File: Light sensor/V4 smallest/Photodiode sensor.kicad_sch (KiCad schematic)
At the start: 11 parts, among them IC1 BH1730FVC-TR, J1 Conn_01x02, J2 Conn_01x04, J3 Conn_01x05

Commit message: Updated footprints
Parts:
- added C1: KAM21BR71H104JM, CAPC2012X94N, symbol CUSTOM_SYMBOL:KAM21BR71H104JM
- added C2: C1608X5R1E475K080AC, CAPC1608X80N, symbol CUSTOM_SYMBOL:C1608X5R1E475K080AC
- R1, R2, R3: value RC0402JR-073M3L -> RMCA1206FT4K70-HP; footprint CUSTOM_LIBRARY:RC0402JR-073M3L -> CUSTOM_LIBRARY:RMCA1206FT4K70-HP
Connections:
- net 3.3V: now also C1.1, C2.1
- net GND: now also C1.2, C2.2
- net INT 2: now also R1.1; no longer R3.1
- net SCL 2: now also R3.1; no longer R1.1

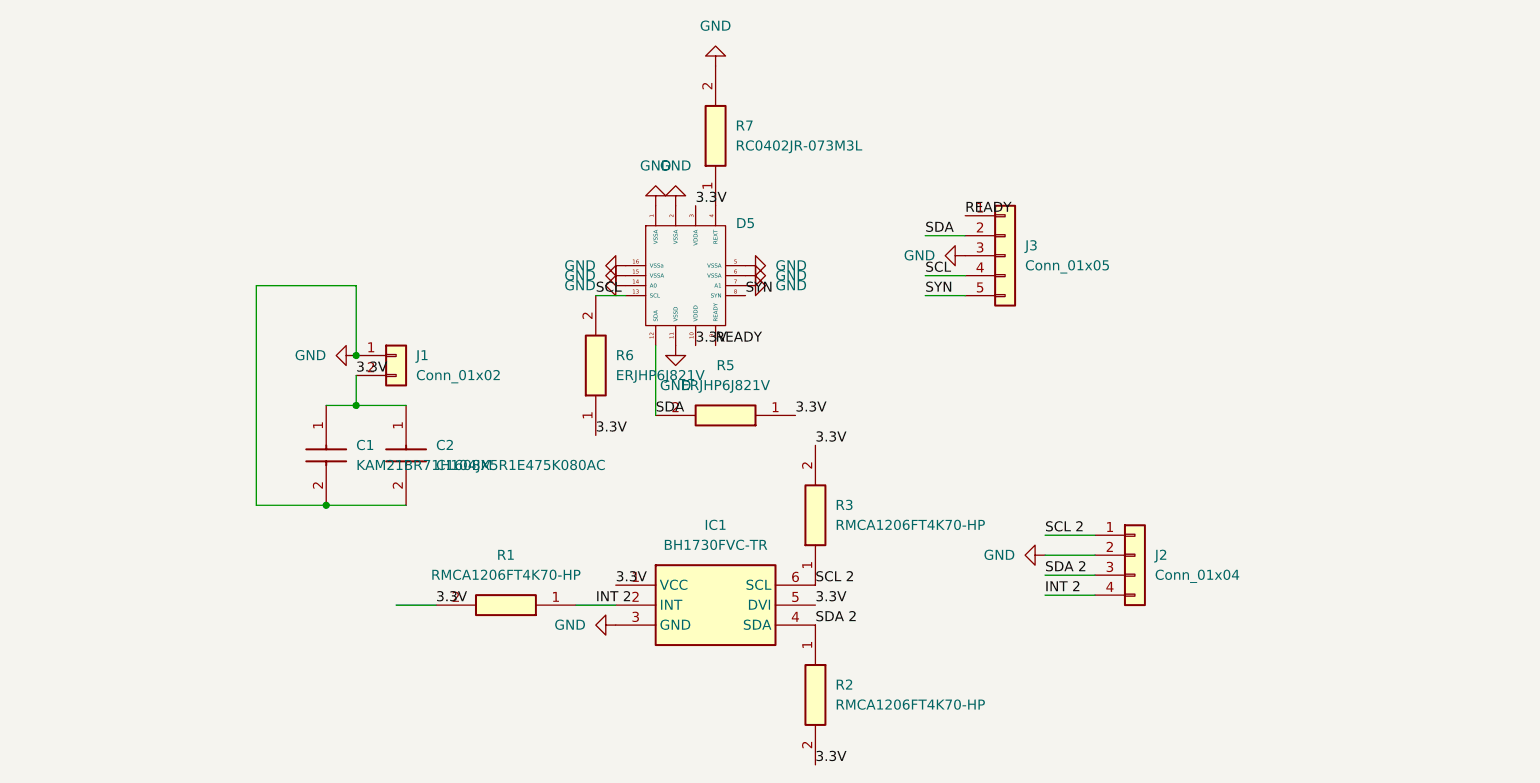
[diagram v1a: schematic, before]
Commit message: Changed V4 PCB
Connected both SCL and SDA pins together as they have different addresses. Made the PCB a lot smaller. Got a good connector placed on the bottom side of the PCB
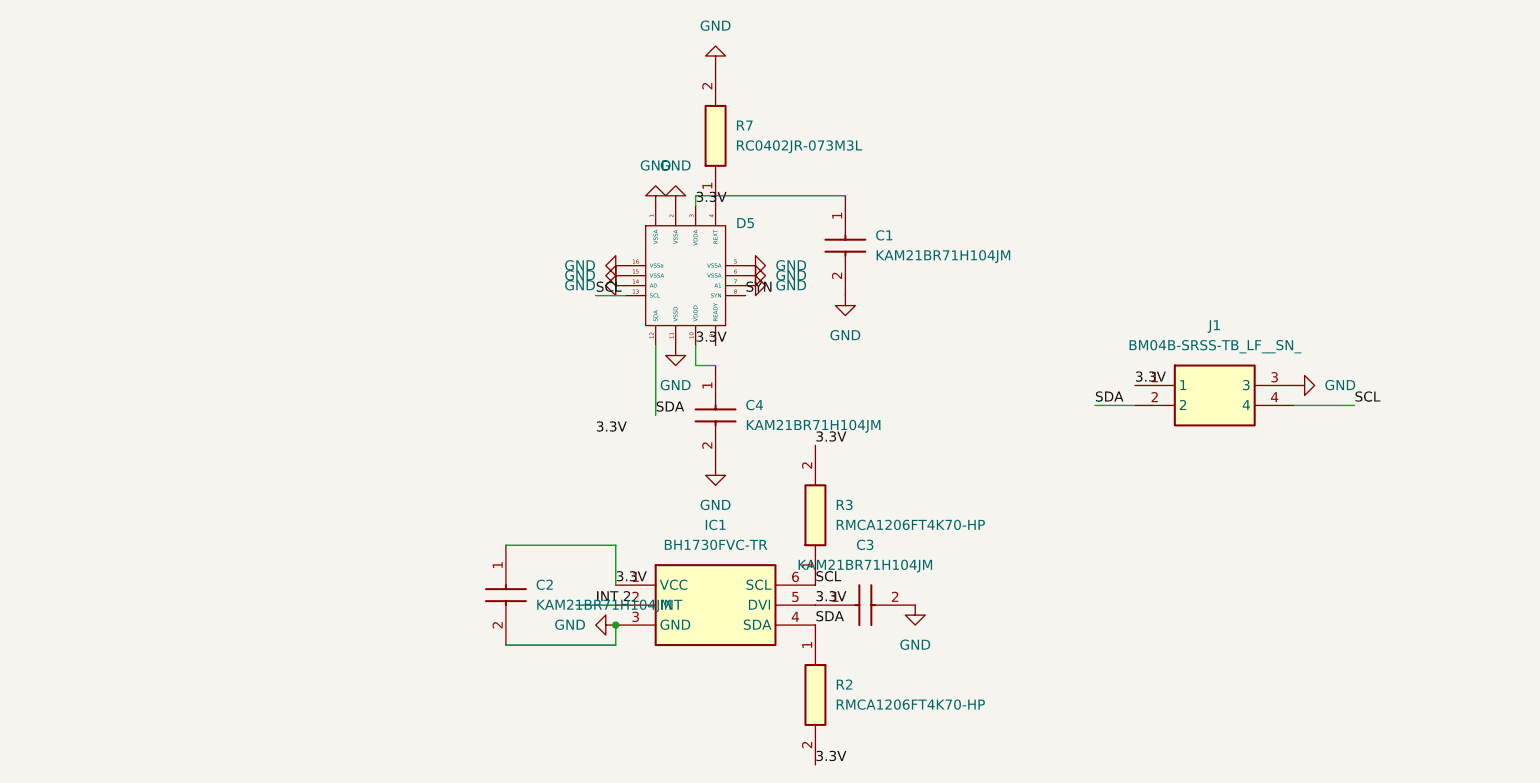
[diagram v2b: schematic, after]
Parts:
- removed C2: C1608X5R1E475K080AC, CAPC1608X80N, symbol CUSTOM_SYMBOL:C1608X5R1E475K080AC
- removed J1: Conn_01x02, Connector_PinHeader_1.00mm:PinHeader_1x02_P1.00mm_Vertical, symbol Connector_Generic:Conn_01x02
- removed J2: Conn_01x04, Connector_PinHeader_1.00mm:PinHeader_1x04_P1.00mm_Vertical, symbol Connector_Generic:Conn_01x04
- removed J3: Conn_01x05, Connector_PinHeader_1.00mm:PinHeader_1x05_P1.00mm_Vertical, symbol Connector_Generic:Conn_01x05
- removed R1: RMCA1206FT4K70-HP, CUSTOM_LIBRARY:RMCA1206FT4K70-HP, symbol CUSTOM_SYMBOL:RMCA1206FT4K70-HP
- removed R5, R6: ERJHP6J821V, ERJHP6D1000V, symbol CUSTOM_SYMBOL:ERJHP6J821V
- added C2, C3, C4: KAM21BR71H104JM, CAPC2012X94N, symbol CUSTOM_SYMBOL:KAM21BR71H104JM
- added J1: BM04B-SRSS-TB_LF__SN_, BM04B-SRSS-TB_LFSN_, symbol CUSTOM_SYMBOL:BM04B-SRSS-TB_LF__SN_
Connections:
- net SCL 2 is gone; now on net SCL: IC1.6 (SCL), R3.1
- net SDA 2 is gone; now on net SDA: IC1.4 (SDA), R2.1
- net 3.3V: now also C2.1, C3.1, C4.1, J1.1
- net GND: now also C2.2, C3.2, C4.2, J1.3
- net SCL: now also J1.4
- net SDA: now also J1.2
- net READY: no longer names the net of D5.9 (READY)
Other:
- moved on the sheet: C1

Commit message: Updated PCB components
Found in stock components and put onto the PCB. Need to double check against datasheet to ensure all connections are good
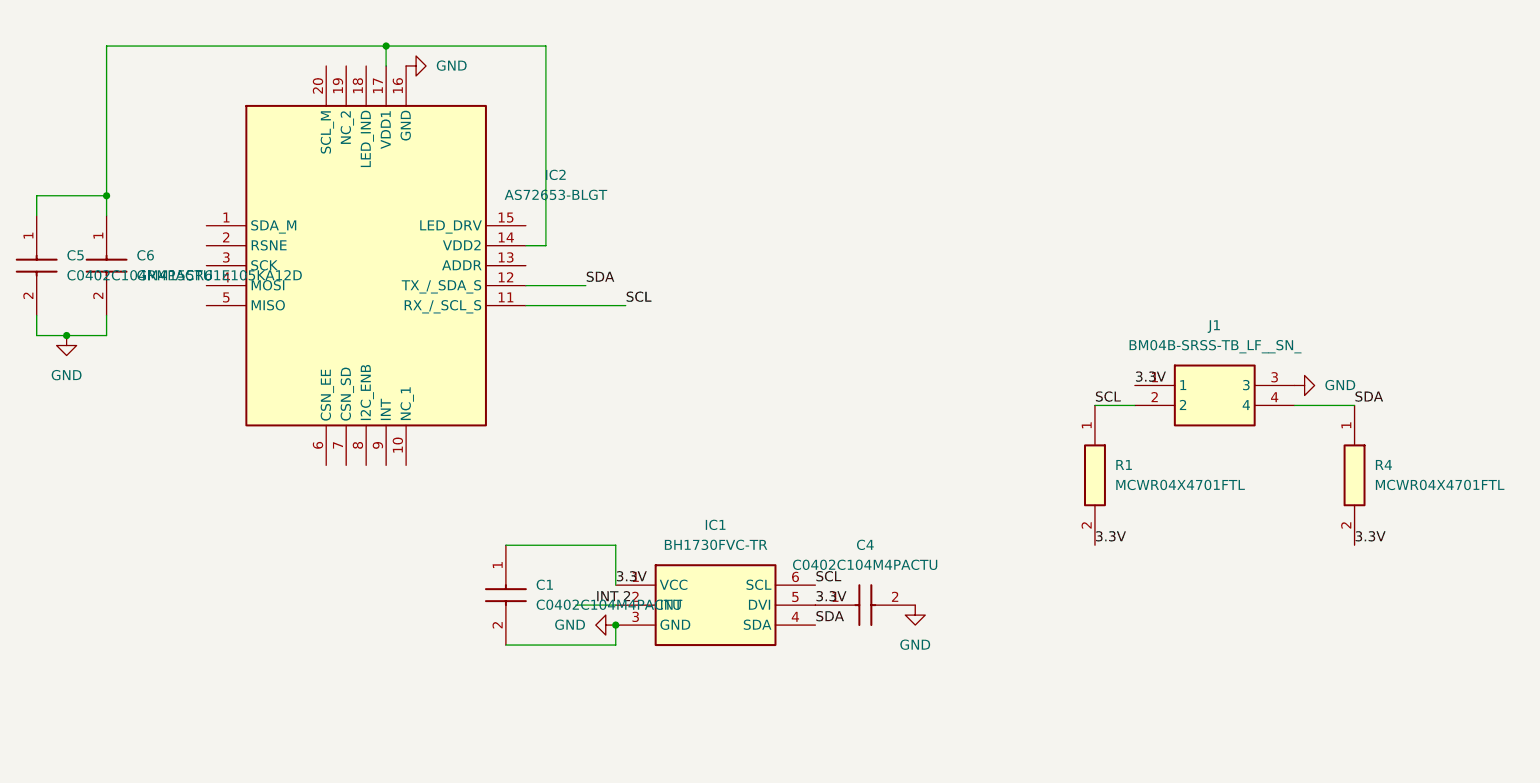
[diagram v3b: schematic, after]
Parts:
- removed C1, C2, C3, C4: KAM21BR71H104JM, CAPC2012X94N, symbol CUSTOM_SYMBOL:KAM21BR71H104JM
- removed D5: ~, CUSTOM_LIBRARY:AS7331-AQFM, symbol CUSTOM_SYMBOL:AS7331-AQFM
- removed IC1: BH1730FVC-TR, WSOF6, symbol CUSTOM_SYMBOL:BH1730FVC-TR
- removed R2, R3: RMCA1206FT4K70-HP, CUSTOM_LIBRARY:RMCA1206FT4K70-HP, symbol CUSTOM_SYMBOL:RMCA1206FT4K70-HP
- removed R7: RC0402JR-073M3L, ERJHP6D1000V, symbol CUSTOM_SYMBOL:RC0402JR-073M3L
- added C1, C4, C5: C0402C104M4PACTU, C0402, symbol SamacSys_Parts:C0402C104M4PACTU
- added C6: GRM155R61E105KA12D, CAPC1005X70N, symbol SamacSys_Parts:GRM155R61E105KA12D
- added IC1: BH1730FVC-TR, BH1730FVCTR, symbol SamacSys_Parts:BH1730FVC-TR
- added IC2: AS72653-BLGT, AS72651BLGT, symbol SamacSys_Parts:AS72653-BLGT
- added R1, R4: MCWR04X4701FTL, RESC1005X40N, symbol SamacSys_Parts:MCWR04X4701FTL
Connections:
- net 3.3V: now also C1.1, C4.1, IC1.1 (VCC), IC1.5 (DVI), R1.2, R4.2
- net GND: now also C1.2, C4.2, C5.2, C6.2, IC1.3 (GND), IC2.16 (GND)
- net INT 2: now also IC1.2 (INT)
- net SCL: now also J1.2, IC1.6 (SCL), IC2.11 (RX_/_SCL_S), R1.1; no longer J1.4
- net SDA: now also J1.4, IC1.4 (SDA), IC2.12 (TX_/_SDA_S), R4.1; no longer J1.2
- new net: C5.1, C6.1, IC2.14 (VDD2), IC2.17 (VDD1)
